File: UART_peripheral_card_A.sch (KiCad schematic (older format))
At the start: 16 parts, among them J1 PP1_edgeConnnector_TE_5-55308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, J2 power_connector, J3 UART_connector, J4 OUTPUT_MODE, U1 74AHC1G32, U2 74AHC1G32, U27 74AHC1G126, U28 74AHC1G126, U3 74AHC1G04, U4 74AHC1G32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

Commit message: Fix active high enable pin #2 by replacing 74AHC1G126 with 74AHC1G125
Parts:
- U27, U28: value 74AHC1G126 -> 74AHC1G125; symbol Custom:74AHC1G126 -> Custom:74AHC1G125
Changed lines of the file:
@@
 RECEIVE_FLAG
 $Comp
-L Custom:74AHC1G126 U27
+L Custom:74AHC1G125 U27
 U 1 1 5FFAFCB2
 P 9500 3550
 F 0 "U27" H 9600 3800 50  0000 L CNN
-F 1 "74AHC1G126" H 9600 3700 50  0000 L CNN
+F 1 "74AHC1G125" H 9600 3700 50  0000 L CNN
 F 2 "Package_TO_SOT_SMD:SOT-23-5" H 9000 4250 50  0001 C CNN
 F 3 "https://www.ti.com/lit/ds/symlink/sn74ahc1g126.pdf" H 9000 4250 50  0001 C CNN
@@
 $EndComp
 $Comp
-L Custom:74AHC1G126 U28
+L Custom:74AHC1G125 U28
 U 1 1 5FFB4059
 P 9500 4700
 F 0 "U28" H 9600 4950 50  0000 L CNN
-F 1 "74AHC1G126" H 9600 4850 50  0000 L CNN
+F 1 "74AHC1G125" H 9600 4850 50  0000 L CNN
 F 2 "Package_TO_SOT_SMD:SOT-23-5" H 9000 5400 50  0001 C CNN
 F 3 "https://www.ti.com/lit/ds/symlink/sn74ahc1g126.pdf" H 9000 5400 50  0001 C CNN

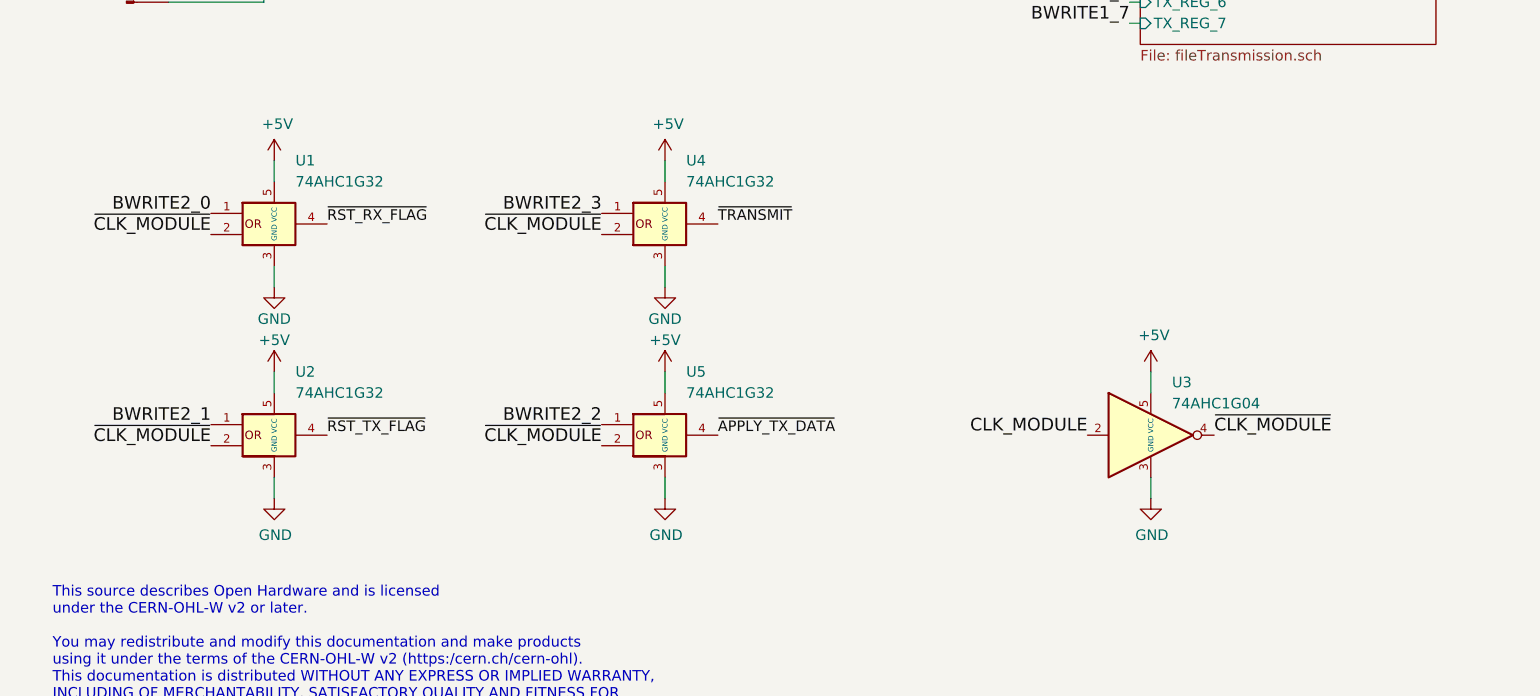
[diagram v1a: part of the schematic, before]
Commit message: Removing the need of U3 inverter #3 replacing U1,U2,U4,U5 with 74AHC1G00
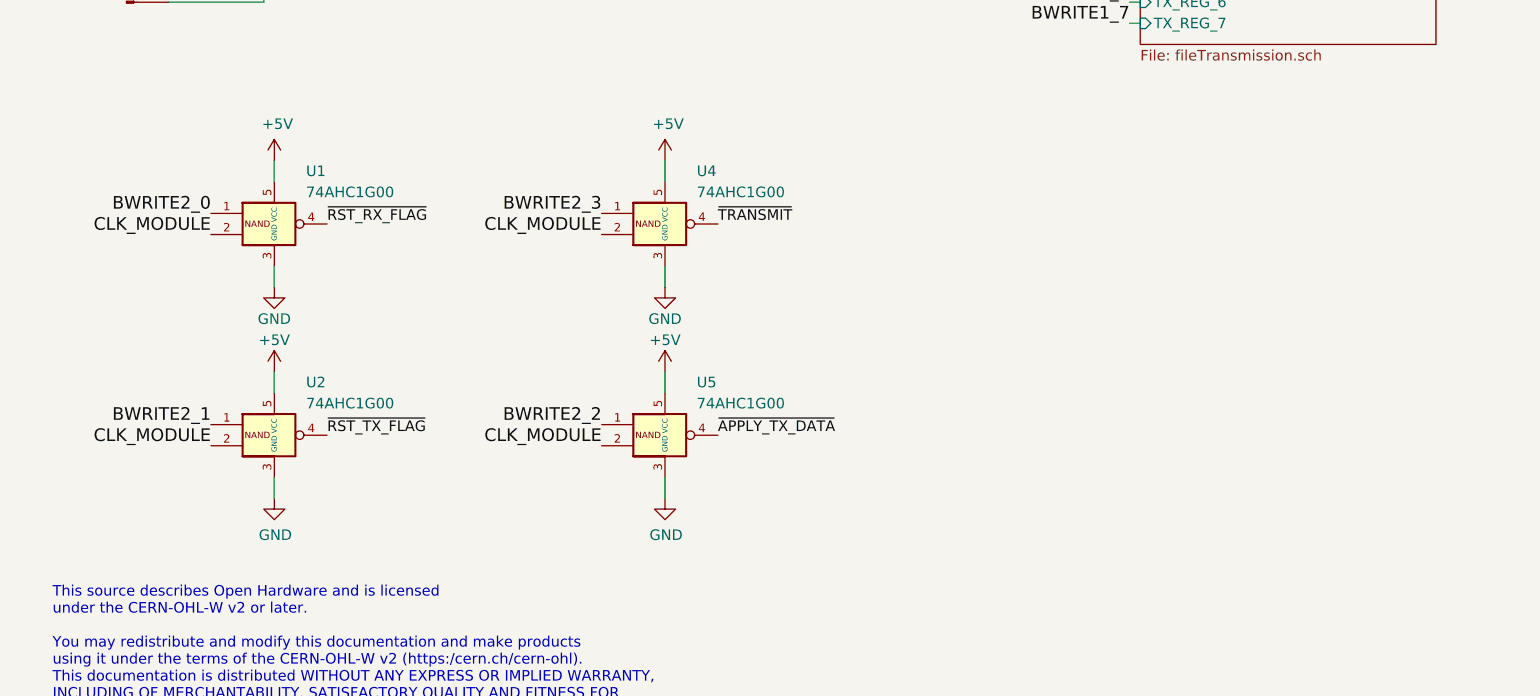
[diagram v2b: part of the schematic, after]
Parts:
- removed U1, U2, U4, U5: 74AHC1G32, Package_TO_SOT_SMD:SOT-23-5, symbol Custom:74AHC1G32
- removed U3: 74AHC1G04, Package_TO_SOT_SMD:SOT-23-5, symbol Custom:74AHC1G04
- added U1, U2, U4, U5: 74AHC1G00, symbol Custom:74AHC1G00
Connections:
- net +5V: now also U1.5 (VCC), U2.5 (VCC), U4.5 (VCC), U5.5 (VCC)
- net BWRITE2_0: now also U1.1
- net BWRITE2_1: now also U2.1
- net BWRITE2_2: now also U5.1
- net BWRITE2_3: now also U4.1
- net CLK_MODULE: now also U1.2, U2.2, U4.2, U5.2
- net GND: now also U1.3 (GND), U2.3 (GND), U4.3 (GND), U5.3 (GND)
- net ~APPLY_TX_DATA: now also U5.4
- net ~RST_RX_FLAG: now also U1.4
- net ~RST_TX_FLAG: now also U2.4
- net ~TRANSMIT: now also U4.4
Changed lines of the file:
@@
 BWRITE2_3
-$Comp
-L Custom:74AHC1G04 U?
-U 1 1 5FFC1020
-P 5850 6100
-AR Path="/5FD66C52/5FFC1020" Ref="U?"  Part="1"
-AR Path="/5FFC1020" Ref="U3"  Part="1"
-F 0 "U3" H 5950 6350 50  0000 L CNN
-F 1 "74AHC1G04" H 5950 6250 50  0000 L CNN
-F 2 "Package_TO_SOT_SMD:SOT-23-5" H 5850 6100 50  0001 C CNN
-F 3 "https://assets.nexperia.com/documents/data-sheet/74AHC_AHCT1G04.pdf" H 5850 6100 50  0001 C CNN
-	1    5850 6100
-	1    0    0    -1
-$EndComp
-$Comp
-L power:+5V #PWR?
-U 1 1 5FFC1026
-P 5850 5800
-AR Path="/5FD66C52/5FFC1026" Ref="#PWR?"  Part="1"
-AR Path="/5FFC1026" Ref="#PWR08"  Part="1"
-F 0 "#PWR08" H 5850 5650 50  0001 C CNN
-F 1 "+5V" H 5865 5973 50  0000 C CNN
-F 2 "" H 5850 5800 50  0001 C CNN
-F 3 "" H 5850 5800 50  0001 C CNN
-	1    5850 5800
-	1    0    0    -1
-$EndComp
-$Comp
-L power:GND #PWR?
-U 1 1 5FFC102C
-P 5850 6400
-AR Path="/5FD66C52/5FFC102C" Ref="#PWR?"  Part="1"
-AR Path="/5FFC102C" Ref="#PWR09"  Part="1"
-F 0 "#PWR09" H 5850 6150 50  0001 C CNN
-F 1 "GND" H 5855 6227 50  0000 C CNN
-F 2 "" H 5850 6400 50  0001 C CNN
-F 3 "" H 5850 6400 50  0001 C CNN
-	1    5850 6400
-	1    0    0    -1
-$EndComp
-Wire Wire Line
-	5850 6300 5850 6400
-Wire Wire Line
-	5850 5900 5850 5800
-Text Label 5550 6100 2    60   ~ 0
-CLK_MODULE
-Text Label 6150 6100 0    60   ~ 0
-~CLK_MODULE
-$Comp
-L Custom:74AHC1G32 U?
-U 1 1 5FFC8798
-P 1700 5100
-AR Path="/5FD66C52/5FFC8798" Ref="U?"  Part="1"
-AR Path="/5FFC8798" Ref="U1"  Part="1"
-F 0 "U1" H 1800 5400 50  0000 L CNN
-F 1 "74AHC1G32" H 1800 5300 50  0000 L CNN
-F 2 "Package_TO_SOT_SMD:SOT-23-5" H 1700 5100 50  0001 C CNN
-F 3 "http://www.ti.com/lit/sg/scyt129e/scyt129e.pdf" H 1700 5100 50  0001 C CNN
-	1    1700 5100
-	1    0    0    -1
-$EndComp
 $Comp
 L power:GND #PWR?
@@
 	1700 4900 1700 4800
 $Comp
-L Custom:74AHC1G32 U?
-U 1 1 5FFCA67F
-P 1700 6100
-AR Path="/5FD66C52/5FFCA67F" Ref="U?"  Part="1"
-AR Path="/5FFCA67F" Ref="U2"  Part="1"
-F 0 "U2" H 1800 6400 50  0000 L CNN
-F 1 "74AHC1G32" H 1800 6300 50  0000 L CNN
-F 2 "Package_TO_SOT_SMD:SOT-23-5" H 1700 6100 50  0001 C CNN
-F 3 "http://www.ti.com/lit/sg/scyt129e/scyt129e.pdf" H 1700 6100 50  0001 C CNN
-	1    1700 6100
-	1    0    0    -1
-$EndComp
-$Comp
 L power:GND #PWR?
 U 1 1 5FFCA685
@@
 	1700 5900 1700 5800
 $Comp
-L Custom:74AHC1G32 U?
-U 1 1 5FFCB043
-P 3550 6100
-AR Path="/5FD66C52/5FFCB043" Ref="U?"  Part="1"
-AR Path="/5FFCB043" Ref="U5"  Part="1"
-F 0 "U5" H 3650 6400 50  0000 L CNN
-F 1 "74AHC1G32" H 3650 6300 50  0000 L CNN
-F 2 "Package_TO_SOT_SMD:SOT-23-5" H 3550 6100 50  0001 C CNN
-F 3 "http://www.ti.com/lit/sg/scyt129e/scyt129e.pdf" H 3550 6100 50  0001 C CNN
-	1    3550 6100
-	1    0    0    -1
-$EndComp
-$Comp
 L power:GND #PWR?
 U 1 1 5FFCB049
@@
 	3550 5900 3550 5800
 $Comp
-L Custom:74AHC1G32 U?
-U 1 1 5FFCB6FE
-P 3550 5100
-AR Path="/5FD66C52/5FFCB6FE" Ref="U?"  Part="1"
-AR Path="/5FFCB6FE" Ref="U4"  Part="1"
-F 0 "U4" H 3650 5400 50  0000 L CNN
-F 1 "74AHC1G32" H 3650 5300 50  0000 L CNN
-F 2 "Package_TO_SOT_SMD:SOT-23-5" H 3550 5100 50  0001 C CNN
-F 3 "http://www.ti.com/lit/sg/scyt129e/scyt129e.pdf" H 3550 5100 50  0001 C CNN
-	1    3550 5100
-	1    0    0    -1
-$EndComp
-$Comp
 L power:GND #PWR?
 U 1 1 5FFCB704
@@
 Wire Wire Line
 	3550 4900 3550 4800
-Text Label 1400 5150 2    60   ~ 0
-~CLK_MODULE
-Text Label 1400 6150 2    60   ~ 0
-~CLK_MODULE
-Text Label 3250 6150 2    60   ~ 0
-~CLK_MODULE
-Text Label 3250 5150 2    60   ~ 0
-~CLK_MODULE
 Text Label 5750 3450 2    60   ~ 0
 BWRITE1_0
@@
 Wire Wire Line
 	10150 2350 10250 2350
+$Comp
+L Custom:74AHC1G00 U1
+U 1 1 609B1DDC
+P 1700 5100
+F 0 "U1" H 1850 5350 50  0000 L CNN
+F 1 "74AHC1G00" H 1850 5250 50  0000 L CNN
+F 2 "" H 1700 5100 50  0001 C CNN
+F 3 "https://assets.nexperia.com/documents/data-sheet/74AHC_AHCT1G00.pdf" H 1700 5100 50  0001 C CNN
+	1    1700 5100
+	1    0    0    -1
+$EndComp
+$Comp
+L Custom:74AHC1G00 U4
+U 1 1 609B49A3
+P 3550 5100
+F 0 "U4" H 3700 5350 50  0000 L CNN
+F 1 "74AHC1G00" H 3700 5250 50  0000 L CNN
+F 2 "" H 3550 5100 50  0001 C CNN
+F 3 "https://assets.nexperia.com/documents/data-sheet/74AHC_AHCT1G00.pdf" H 3550 5100 50  0001 C CNN
+	1    3550 5100
+	1    0    0    -1
+$EndComp
+$Comp
+L Custom:74AHC1G00 U5
+U 1 1 609B4F12
+P 3550 6100
+F 0 "U5" H 3700 6350 50  0000 L CNN
+F 1 "74AHC1G00" H 3700 6250 50  0000 L CNN
+F 2 "" H 3550 6100 50  0001 C CNN
+F 3 "https://assets.nexperia.com/documents/data-sheet/74AHC_AHCT1G00.pdf" H 3550 6100 50  0001 C CNN
+	1    3550 6100
+	1    0    0    -1
+$EndComp
+$Comp
+L Custom:74AHC1G00 U2
+U 1 1 609B5381
+P 1700 6100
+F 0 "U2" H 1850 6350 50  0000 L CNN
+F 1 "74AHC1G00" H 1850 6250 50  0000 L CNN
+F 2 "" H 1700 6100 50  0001 C CNN
+F 3 "https://assets.nexperia.com/documents/data-sheet/74AHC_AHCT1G00.pdf" H 1700 6100 50  0001 C CNN
+	1    1700 6100
+	1    0    0    -1
+$EndComp
+Text Label 3250 5150 2    60   ~ 0
+CLK_MODULE
+Text Label 3250 6150 2    60   ~ 0
+CLK_MODULE
+Text Label 1400 6150 2    60   ~ 0
+CLK_MODULE
+Text Label 1400 5150 2    60   ~ 0
+CLK_MODULE
 $EndSCHEMATC

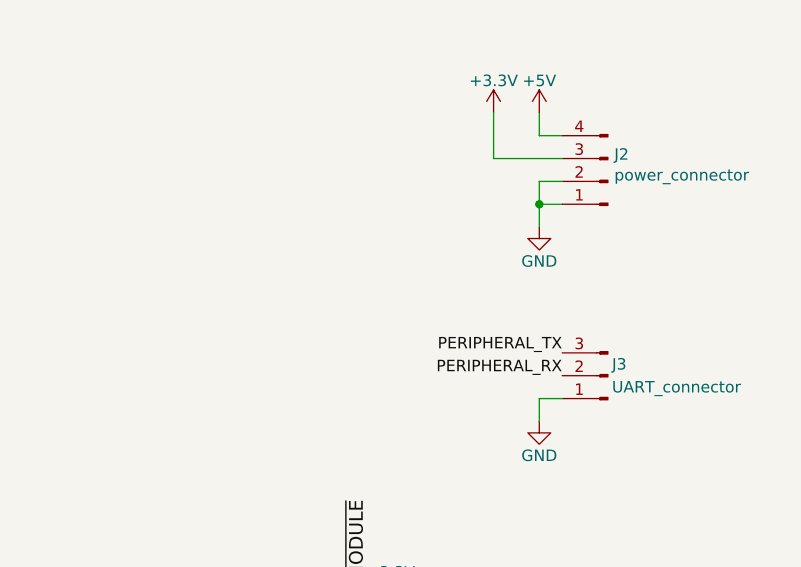
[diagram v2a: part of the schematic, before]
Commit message: Adding pull-up on RX pin #4
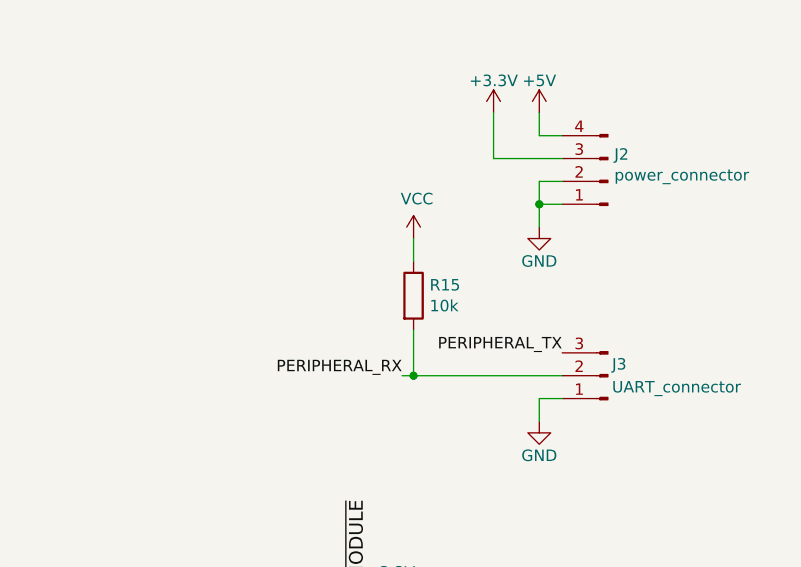
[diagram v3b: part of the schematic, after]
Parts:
- added R15: 10k, Resistor_SMD:R_0805_2012Metric, symbol Device:R
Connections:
- net PERIPHERAL_RX: now also R15.2
- net VCC: now also R15.1
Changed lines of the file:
@@
 Text Label 10250 2150 2    50   ~ 0
 PERIPHERAL_TX
-Text Label 10250 2250 2    50   ~ 0
+Text Label 9550 2250 2    50   ~ 0
 PERIPHERAL_RX
 $Sheet
@@
 Text Label 1400 5150 2    60   ~ 0
 CLK_MODULE
+$Comp
+L Device:R R?
+U 1 1 609C4D0A
+P 9600 1900
+AR Path="/5FD66C52/609C4D0A" Ref="R?"  Part="1"
+AR Path="/609C4D0A" Ref="R15"  Part="1"
+F 0 "R15" H 9670 1946 50  0000 L CNN
+F 1 "10k" H 9670 1855 50  0000 L CNN
+F 2 "Resistor_SMD:R_0805_2012Metric" V 9530 1900 50  0001 C CNN
+F 3 "~" H 9600 1900 50  0001 C CNN
+	1    9600 1900
+	1    0    0    -1
+$EndComp
+Wire Wire Line
+	9600 2050 9600 2250
+Wire Wire Line
+	9600 2250 9550 2250
+Wire Wire Line
+	9600 2250 10250 2250
+Connection ~ 9600 2250
+$Comp
+L power:VCC #PWR0109
+U 1 1 609CB94C
+P 9600 1650
+F 0 "#PWR0109" H 9600 1500 50  0001 C CNN
+F 1 "VCC" H 9615 1823 50  0000 C CNN
+F 2 "" H 9600 1650 50  0001 C CNN
+F 3 "" H 9600 1650 50  0001 C CNN
+	1    9600 1650
+	1    0    0    -1
+$EndComp
+Wire Wire Line
+	9600 1750 9600 1650
 $EndSCHEMATC
